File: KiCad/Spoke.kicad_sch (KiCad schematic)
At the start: 135 parts, among them J1 B2B-PH-K-S, J10 BL-A, J11 BL-C, J12 Amphenol 132289, J2 BAT+, J3 BAT-, J4 GCT USB4105/USB4110, J5 USB+, J6 USB-, J7 PLS-1x3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

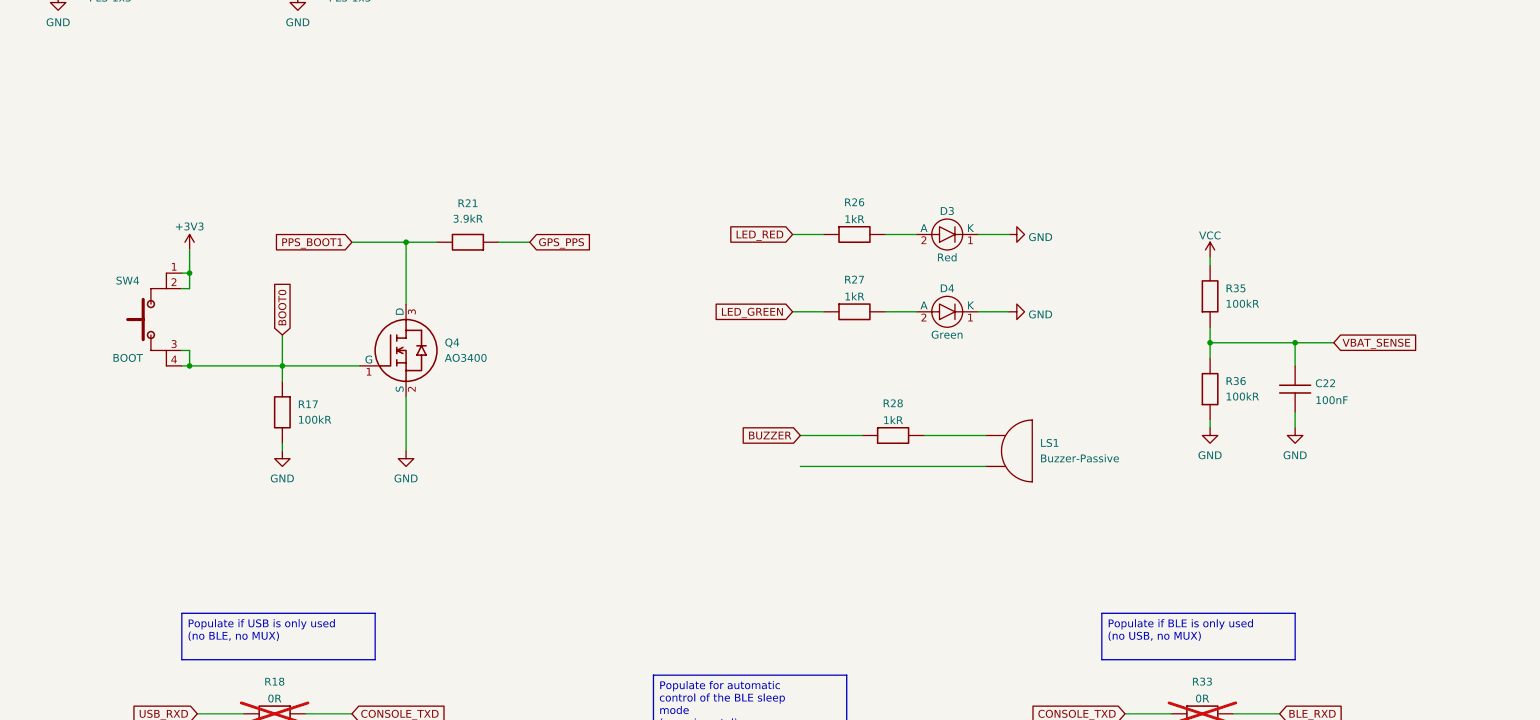
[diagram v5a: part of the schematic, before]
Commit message: Draw buzzer drive circuit
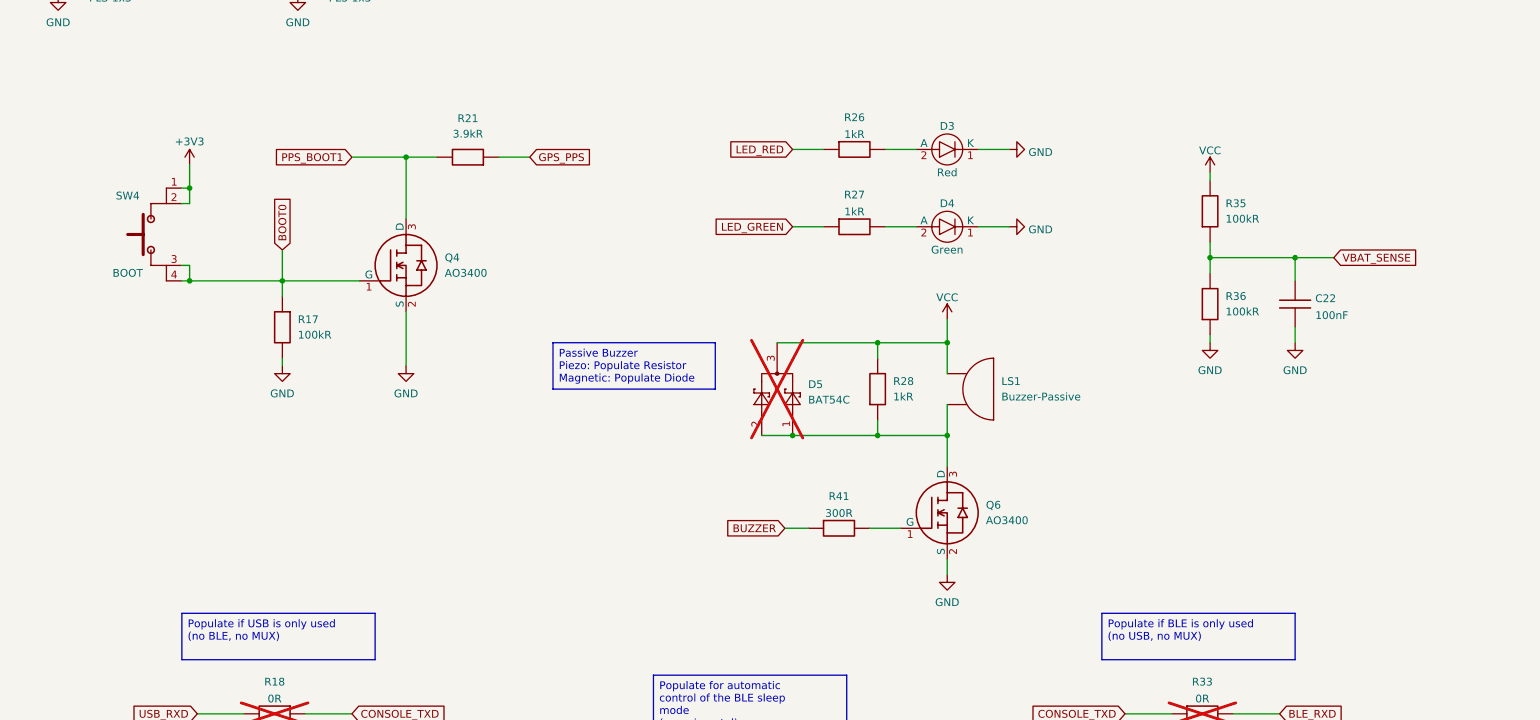
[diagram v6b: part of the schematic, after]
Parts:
- added D5: BAT54C, Spoke:SOT-23, symbol Spoke:BAT54C
- added Q6: AO3400, Spoke:SOT-23, symbol Spoke:NMOS
- added R41: 300R, Spoke:R0603, symbol Spoke:R
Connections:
- net BUZZER: now also R41.1; no longer R28.1
- net GND: now also Q6.2 (S)
- net VCC: now also LS1.1, R28.2, D5.3
- net at LS1.2: now also R28.1, D5.1, D5.2, Q6.3 (D)
- new net: Q6.1 (G), R41.2
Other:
- moved on the sheet: C22, D3, D4, LS1, Q4, R17, R21, R26, R27, R28, R35, R36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

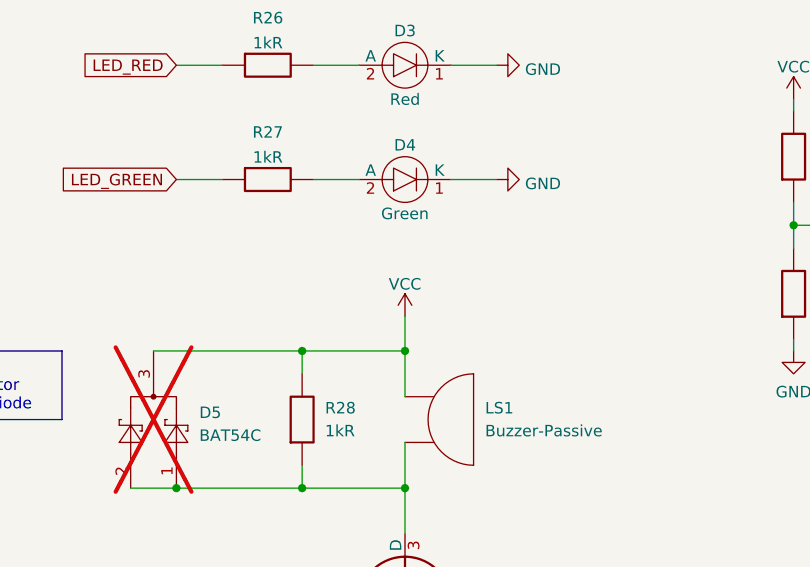
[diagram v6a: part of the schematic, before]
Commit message: Route buzzer circuit
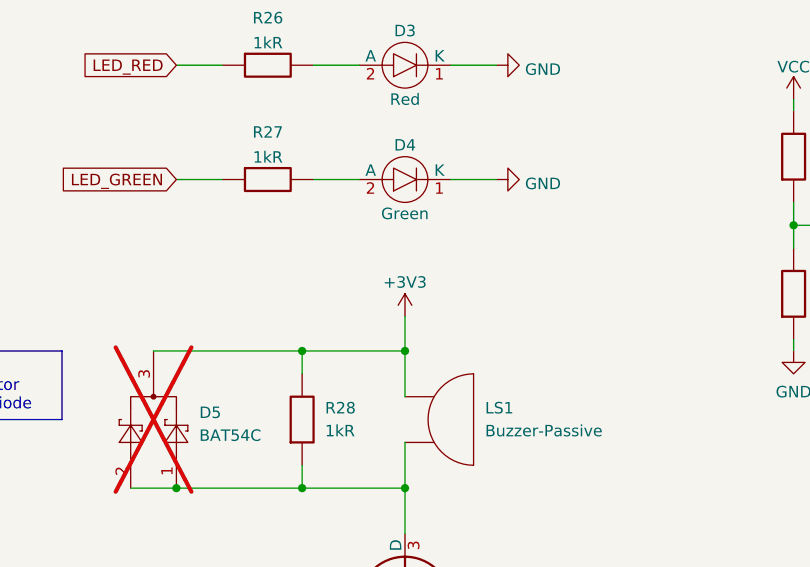
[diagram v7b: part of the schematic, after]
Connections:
- net +3V3: now also D5.3, LS1.1, R28.2
- net VCC: no longer D5.3, LS1.1, R28.2
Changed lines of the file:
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@@
 	)
 	(symbol
-		(lib_id "power:VCC")
-		(at 341.63 217.17 0)
-		(unit 1)
-		(exclude_from_sim no)
-		(in_bom yes)
-		(on_board yes)
-		(dnp no)
-		(fields_autoplaced yes)
-		(property "Reference" "#PWR0106"
-			(at 341.63 220.98 0)
-			(effects
-				(font
-					(size 1.27 1.27)
-				)
-				(hide yes)
-			)
-		)
-		(property "Value" "VCC"
-			(at 341.63 213.5655 0)
-			(effects
-				(font
-					(size 1.27 1.27)
-				)
-			)
-		)
-		(property "Footprint" ""
-			(at 341.63 217.17 0)
-			(effects
-				(font
-					(size 1.27 1.27)
-				)
-				(hide yes)
-			)
-		)
-		(property "Datasheet" ""
-			(at 341.63 217.17 0)
-			(effects
-				(font
-					(size 1.27 1.27)
-				)
-				(hide yes)
-			)
-		)
-		(property "Description" ""
-			(at 341.63 217.17 0)
-			(effects
-				(font
-					(size 1.27 1.27)
-				)
-			)
-		)
-		(pin "1"
-		)
-		(instances
-			(project "Spoke"
-				(path "/e63e39d7-6ac0-4ffd-8aa3-1841a4541b55"
-					(reference "#PWR0106")
-					(unit 1)
-				)
-			)
-		)
-	)
-	(symbol
 		(lib_id "power:GND")
 		(at 537.21 293.37 0)
@@
 					(unit 1)
 				)
+			)
+		)
+	)
+	(symbol
+		(lib_id "power:+3V3")
+		(at 341.63 217.17 0)
+		(unit 1)
+		(exclude_from_sim no)
+		(in_bom yes)
+		(on_board yes)
+		(dnp no)
+		(property "Reference" "#PWR0108"
+			(at 341.63 220.98 0)
+			(effects
+				(font
+					(size 1.27 1.27)
+				)
+				(hide yes)
+			)
+		)
+		(property "Value" "+3V3"
+			(at 341.63 213.36 0)
+			(effects
+				(font
+					(size 1.27 1.27)
+				)
+			)
+		)
+		(property "Footprint" ""
+			(at 341.63 217.17 0)
+			(effects
+				(font
+					(size 1.27 1.27)
+				)
+				(hide yes)
+			)
+		)
+		(property "Datasheet" ""
+			(at 341.63 217.17 0)
+			(effects
+				(font
+					(size 1.27 1.27)
+				)
+				(hide yes)
+			)
+		)
+		(property "Description" "Power symbol creates a global label with name \"+3V3\""
+			(at 341.63 217.17 0)
+			(effects
+				(font
+					(size 1.27 1.27)
+				)
+				(hide yes)
+			)
+		)
+		(pin "1"
+		)
+		(instances
+			(project "Spoke"
+				(path "/e63e39d7-6ac0-4ffd-8aa3-1841a4541b55"
+					(reference "#PWR0108")
+					(unit 1)
+				)

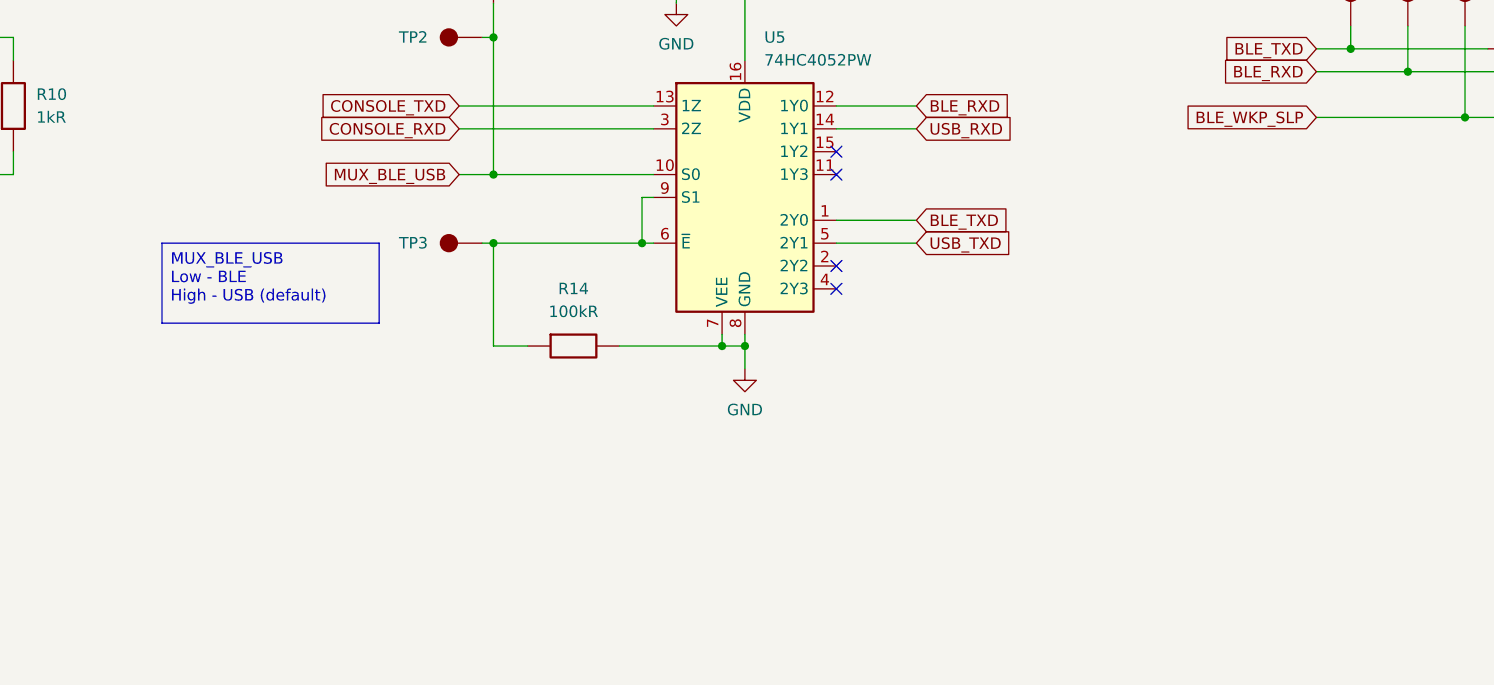
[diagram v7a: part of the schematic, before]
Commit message: Wire GPS to MUX
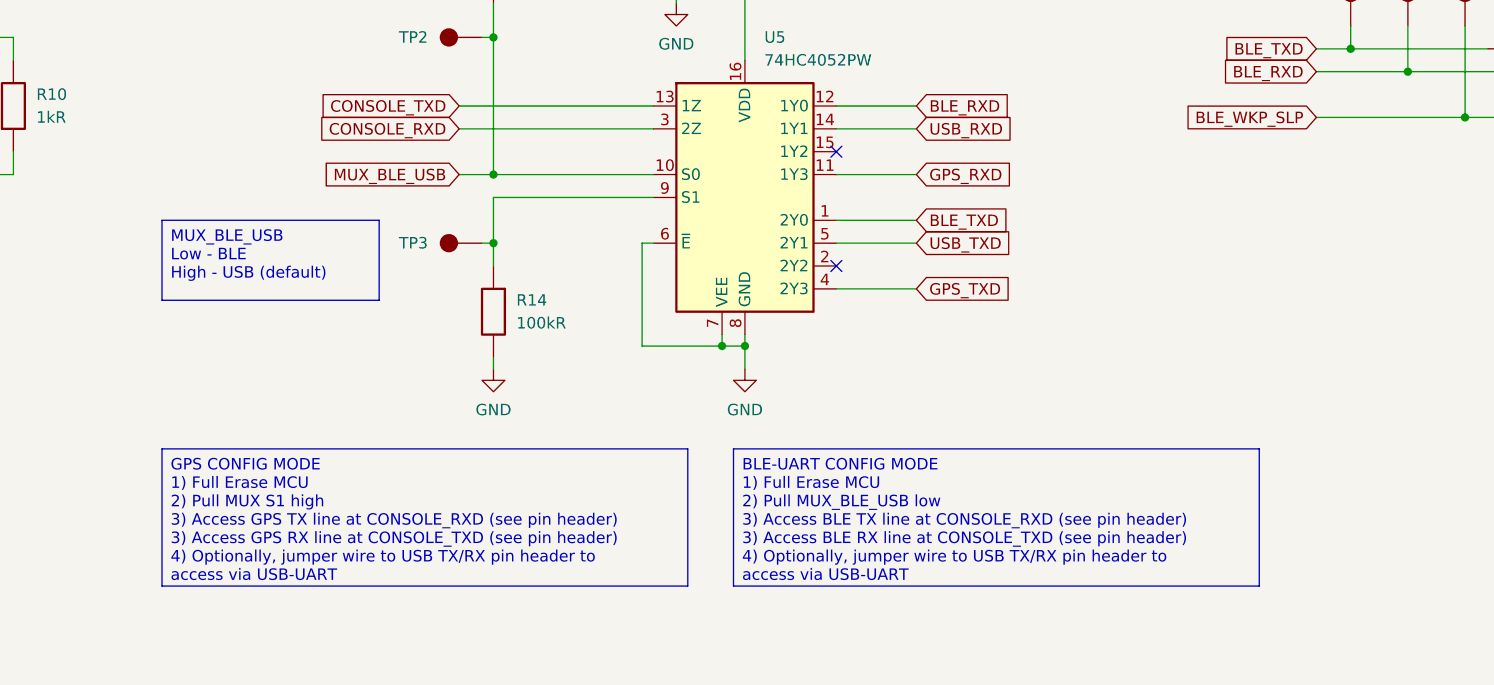
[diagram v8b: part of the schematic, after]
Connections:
- net GND: now also U5.6 (~{E})
- net GPS_RXD: now also U5.11 (1Y3)
- net GPS_TXD: now also U5.4 (2Y3)
- net at R14.1, TP3.1, U5.9 (S1): no longer U5.6 (~{E})
- no-connect marks 34 -> 32
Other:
- moved on the sheet: R14
